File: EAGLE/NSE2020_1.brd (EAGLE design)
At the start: 80 x 80 mm, 46 parts, among them CN1 MICROSD, IC1 ADP3338-3.3, X1 MINI-USB-UX60A-MB-5ST

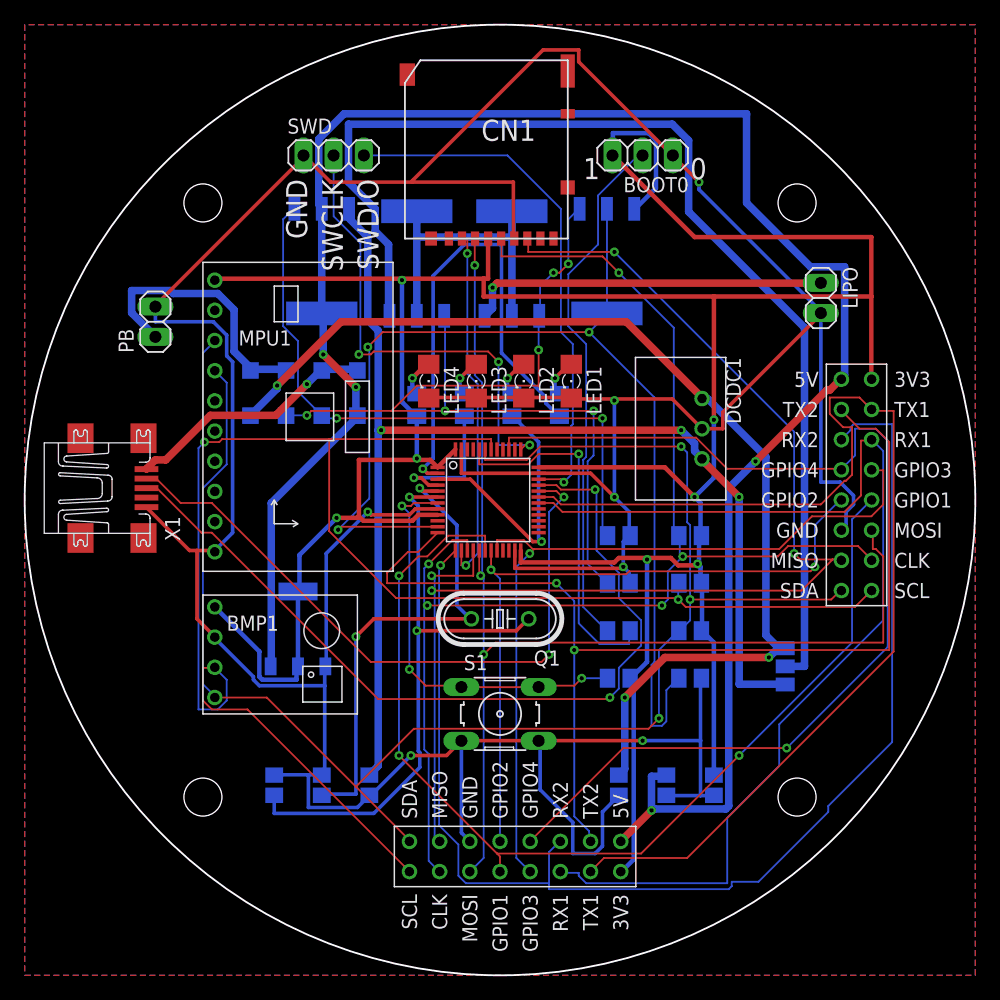
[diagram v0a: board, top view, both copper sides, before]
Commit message: camファイルとデザインルール等を追加
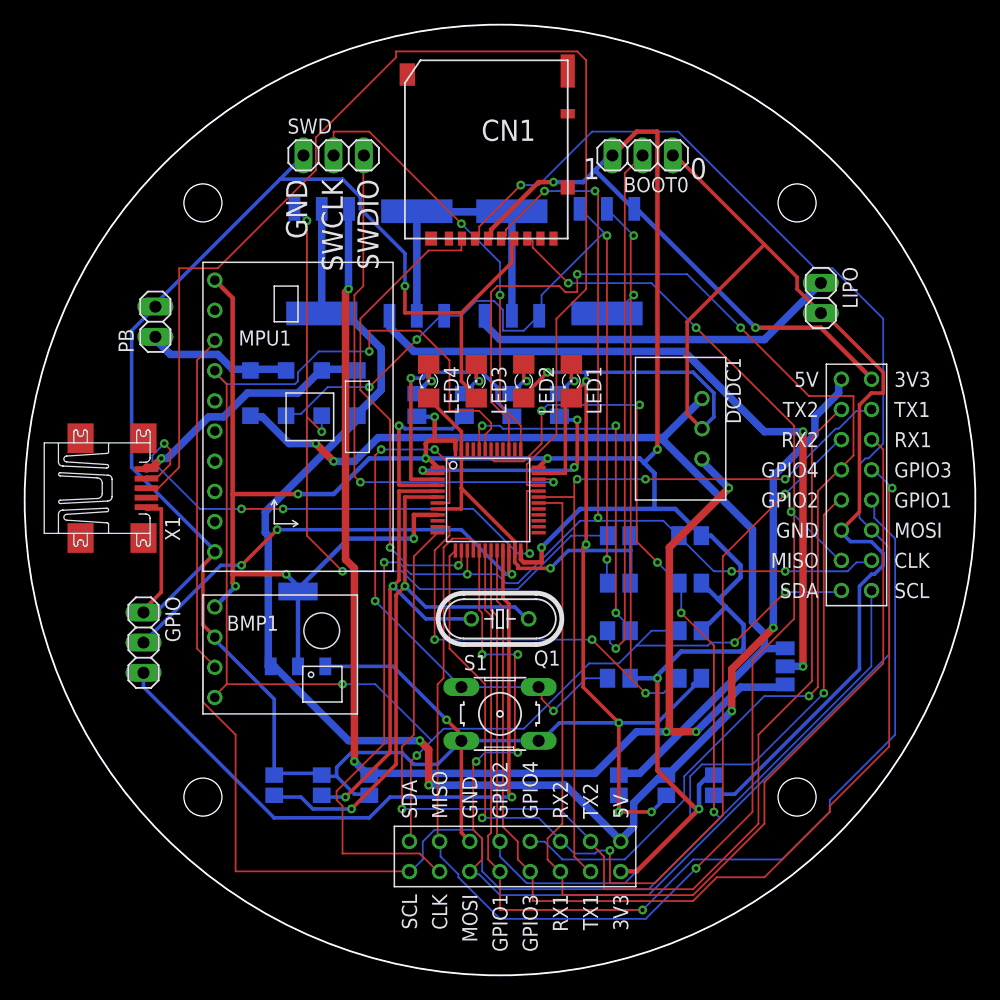
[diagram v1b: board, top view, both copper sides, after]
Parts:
- added GPIO: (no value), pinhead:1X03
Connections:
- new net RX_3: GPIO.2, MCU1.22
- new net TX_3: GPIO.3, MCU1.21
- net GND: now also GPIO.1
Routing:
- net TX_3: track 0.00 -> 58.6 mm, vias 0 -> 1
- net MOSI: track 100.6 -> 154.1 mm, vias 3 -> 5
- net RX_3: track 0.00 -> 38.6 mm, vias 0 -> 3
- net +5V: track 167.7 -> 130.8 mm
- net FET2JUMP: track 96.7 -> 60.7 mm, vias 0 -> 2
- net GND: track 360.0 -> 394.2 mm, vias 7 -> 9
- net DP: track 71.5 -> 103.1 mm, vias 2 -> 0
- net TX_1: track 94.7 -> 64.0 mm, vias 0 -> 3
- net SCL: track 147.9 -> 176.6 mm, vias 2 -> 5
- net MISO: track 107.6 -> 131.8 mm
- net GPIO3: track 67.4 -> 90.6 mm
- net IO2LED1: track 41.4 -> 20.1 mm, vias 1 -> 3
- net GPIO2: track 59.1 -> 79.9 mm, vias 2 -> 1
- net RX_2: track 107.2 -> 86.6 mm, vias 1 -> 3
- net PBDET: track 96.1 -> 77.7 mm, vias 3 -> 5
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- removed copper zone on layer 1, net GND
- removed copper zone on layer 16, net GND
